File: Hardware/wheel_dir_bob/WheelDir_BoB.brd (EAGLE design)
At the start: 15 parts, among them U1 DUAL-OPTOISOLATOR_SOIC8

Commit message: Deletes uneccessary optoisolator
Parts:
- removed U1: DUAL-OPTOISOLATOR_SOIC8, SparkFun-DiscreteSemi:SO08
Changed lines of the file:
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@@
 <attribute name="VALUE" x="-10.16" y="-68.072" size="0.6096" layer="27" font="vector" ratio="20" align="top-center"/>
-</element>
-<element name="U1" library="SparkFun-DiscreteSemi" package="SO08" value="DUAL-OPTOISOLATOR_SOIC8" x="-7.62" y="-72.39" smashed="yes">
-<attribute name="NAME" x="-10.795" y="-72.39" size="0.6096" layer="25" font="vector" ratio="20" rot="R90" align="bottom-center"/>
-<attribute name="PROD_ID" value="IC-09076" x="-7.62" y="-72.39" size="1.778" layer="27" font="vector" ratio="15" display="off"/>
-<attribute name="VALUE" x="-3.81" y="-72.39" size="0.6096" layer="27" font="vector" ratio="20" rot="R90" align="bottom-center"/>
 </element>
 <element name="D1" library="SparkFun-DiscreteSemi" package="SOD-323" value="0.5A/40V/420mV" x="-8.89" y="-81.28" smashed="yes">

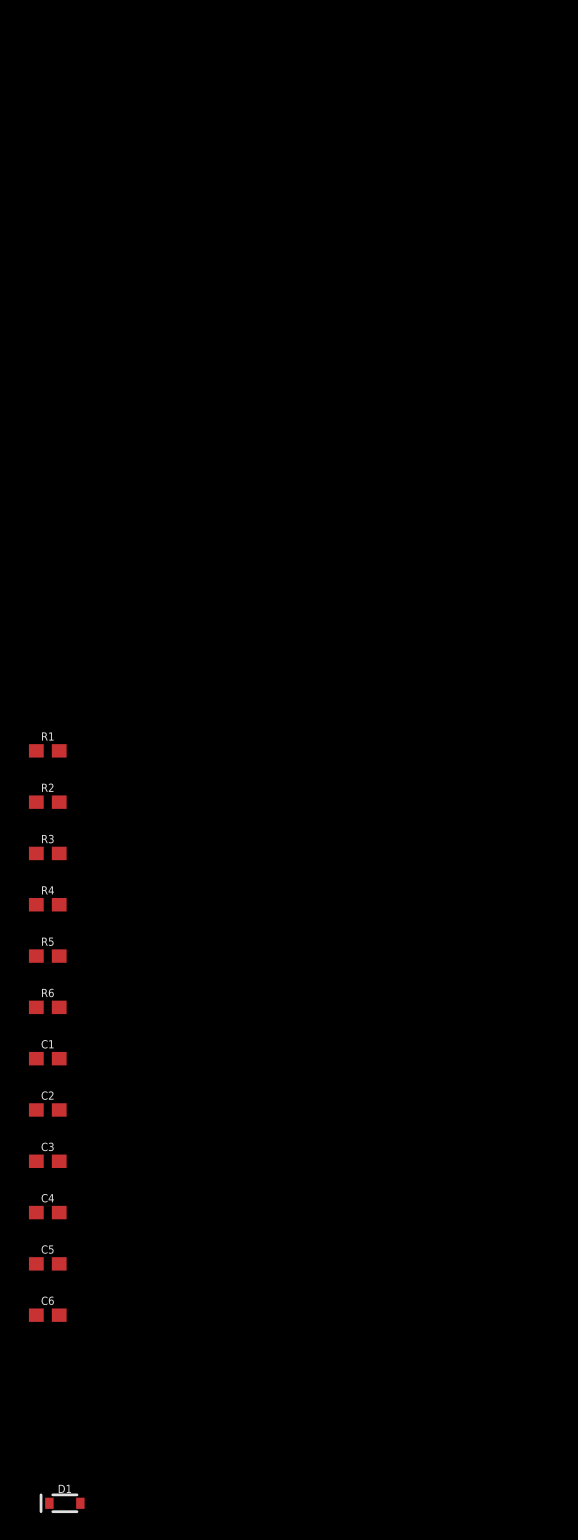
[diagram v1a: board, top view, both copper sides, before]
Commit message: Adds the automotive interface breakout board
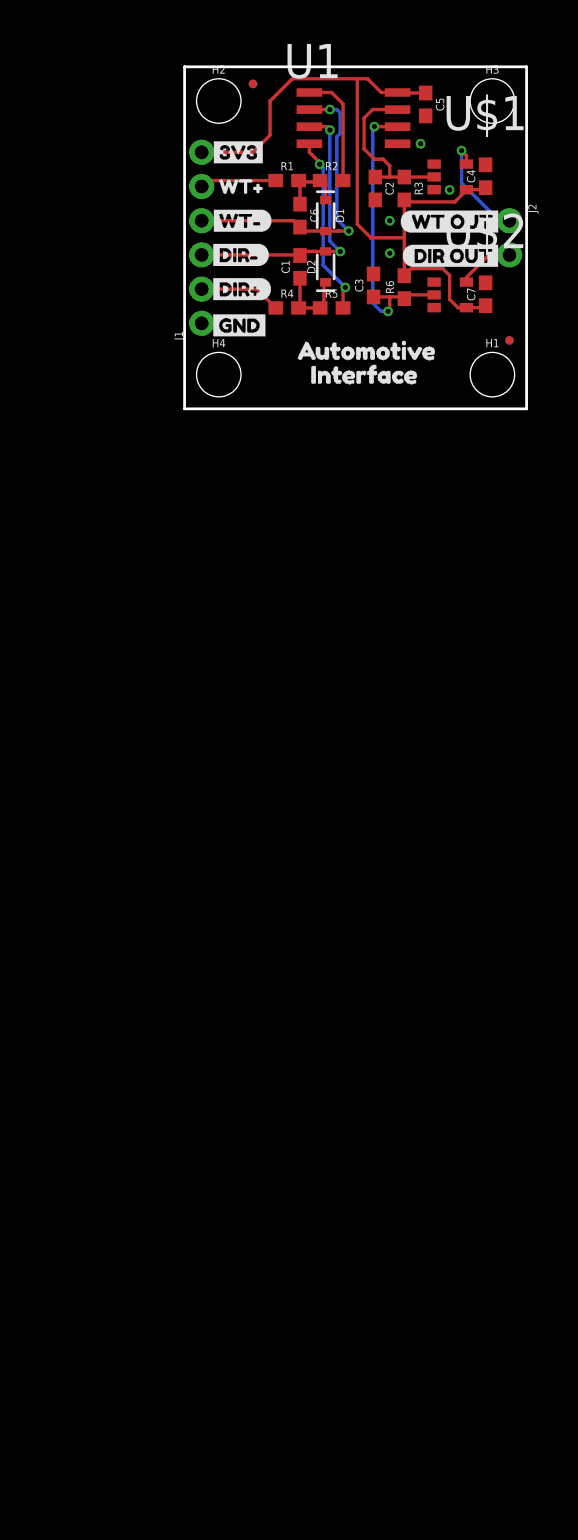
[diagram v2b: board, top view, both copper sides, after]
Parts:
- added C7: 100nF, classified:0603
- added D2: 0.5A/40V/420mV, SparkFun-DiscreteSemi:SOD-323
- added FD1, FD2, FD3, FD4: FIDUCIALUFIDUCIAL, SparkFun-Aesthetics:FIDUCIAL-MICRO
- added H1, H2, H3, H4: STAND-OFF, SparkFun-Hardware:STAND-OFF
- added J1: (no value), SparkFun-Connectors:1X06_NO_SILK
- added J2: (no value), SparkFun-Connectors:1X02_NO_SILK
- added LOGO1: SFE_LOGO_NAME_FLAME.1_INCH, SparkFun-Aesthetics:SFE_LOGO_NAME_FLAME_.1
- added LOGO2: OSHW-LOGOS, SparkFun-Aesthetics:OSHW-LOGO-S
- added U$1, U$2: UHS_INVERTER_SCHMITT_TRIGGER, classified:SC-74A
- added U$10: (no value), main_labels:INTERFACE7
- added U$11, U$3: (no value), main_labels:DIR#2
- added U$12, U$4: (no value), main_labels:DIR#3
- added U$13, U$8: (no value), main_labels:DIR_OUT5
- added U$14: (no value), main_labels:WT#0
- added U$15, U$5: (no value), main_labels:WT#1
- added U$16, U$7: (no value), main_labels:WT_OUT4
- added U$17, U$19: (no value), Labels:3V3-04
- added U$18, U$20: (no value), Labels:GND-04
- added U$6: (no value), wt:WT#0
- added U$9: (no value), main_labels:AUTOMOTIVE6
- added U1: HCPL-270L, classified:SOP_8-PIN
- C4, C5: value 100pF -> 100nF; device SparkFun-Capacitors:0603 -> classified:0603
- R3, R6: value 866 -> 910; device SparkFun-Resistors:0603 -> classified:0603
- moved D1 97.6 mm to (10.5, 14.4), turned to 270 degrees
- moved C5 90.6 mm to (17.9, 22.6), turned to 270 degrees
- moved C6 83.8 mm to (8.57, 14.4), turned to 270 degrees
- moved C4 83.5 mm to (22.4, 17.3), turned to 90 degrees
- moved C2 72.6 mm to (14.2, 16.4), turned to 270 degrees
- moved C3 69.4 mm to (14.0, 9.16), turned to 90 degrees
- moved C1 61.7 mm to (8.57, 10.5), turned to 90 degrees
- moved R6 59.7 mm to (16.3, 9.04), turned to 90 degrees
- moved R3 56.0 mm to (16.3, 16.4), turned to 270 degrees
- moved R5 52.5 mm to (10.9, 7.49)
- moved R2 50.8 mm to (10.9, 17.0)
- moved R4 47.8 mm to (7.62, 7.49)
- moved R1 45.9 mm to (7.62, 17.0)
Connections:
- new net 3.3V: C4.1, C5.1, C7.1, J1.6, R3.2, R6.2, U$1.P5, U$2.P5, U1.P8
- new net DIR+: J1.2, R4.1
- new net DIR-: C1.2, D2.A, J1.3, U1.P3
- new net DIR_IN: R5.2, U1.P4
- new net DIR_SCHMITT: C3.1, R6.1, U$2.P2, U1.P6
- new net DIR_U-BLOX: J2.2, U$2.P4
- new net GND: C2.2, C3.2, C4.2, C5.2, C7.2, J1.1, U$1.P3, U$2.P3, U1.P5
- new net N$2: C6.1, D1.C, R1.2, R2.1
- new net N$3: C1.1, D2.C, R4.2, R5.1
- new net WT+: J1.5, R1.1
- new net WT-: C6.2, D1.A, J1.4, U1.P2
- new net WT_IN: R2.2, U1.P1
- new net WT_SCHMITT: C2.1, R3.1, U$1.P2, U1.P7
- new net WT_U-BLOX: J2.1, U$1.P4
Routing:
- net 3.3V: track 0.00 -> 56.3 mm
- net WT-: track 0.00 -> 22.9 mm, vias 0 -> 2
- net DIR_SCHMITT: track 0.00 -> 22.1 mm, vias 0 -> 2
- net DIR-: track 0.00 -> 21.4 mm, vias 0 -> 2
- net DIR_IN: track 0.00 -> 13.4 mm, vias 0 -> 2
- net WT_SCHMITT: track 0.00 -> 12.9 mm
- net WT_IN: track 0.00 -> 8.54 mm
- net WT_U-BLOX: track 0.00 -> 8.28 mm, vias 0 -> 1
- net N$3: track 0.00 -> 6.18 mm
- net DIR+: track 0.00 -> 6.08 mm
- net WT+: track 0.00 -> 5.68 mm
- net N$2: track 0.00 -> 5.20 mm
- net DIR_U-BLOX: track 0.00 -> 4.23 mm
- added copper zone on layer 1, net GND
- added copper zone on layer 16, net GND
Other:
- board outline added: 25.4 x 25.4 mm
